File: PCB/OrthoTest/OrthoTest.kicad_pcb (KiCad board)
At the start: 2 copper layers, 233.7 x 127.2 mm, 249 parts, among them SW1 SW_Push, SW10 SW_Push, SW11 SW_Push, SW12 SW_Push, SW13 SW_Push, SW14 SW_Push, SW15 SW_Push, SW16 SW_Push, SW17 SW_Push, SW18 SW_Push, SW19 SW_Push, SW2 SW_Push, SW20 SW_Push, SW21 SW_Push, SW22 SW_Push, SW23 SW_Push, SW24 SW_Push, SW25 SW_Push, SW26 SW_Push, SW27 SW_Push, SW28 SW_Push, SW29 SW_Push, SW3 SW_Push, SW30 SW_Push, SW31 SW_Push, SW32 SW_Push, SW33 SW_Push, SW34 SW_Push, SW35 SW_Push, SW36 SW_Push, SW37 SW_Push, SW38 SW_Push, SW39 SW_Push, SW4 SW_Push, SW40 SW_Push, SW41 SW_Push, SW42 SW_Push, SW43 SW_Push, SW44 SW_Push, SW45 SW_Push, SW46 SW_Push, SW47 SW_Push, SW48 SW_Push, SW49 SW_Push, SW5 SW_Push, SW50 SW_Push, SW51 SW_Push, SW52 SW_Push, SW53 SW_Push, SW54 SW_Push, SW55 SW_Push, SW56 SW_Push, SW57 SW_Push, SW58 SW_Push, SW59 SW_Push, SW6 SW_Push, SW60 RotaryEncoder_Switch_MP, SW61 RotaryEncoder_Switch_MP, SW7 SW_Push, SW8 SW_Push, SW9 SW_Push

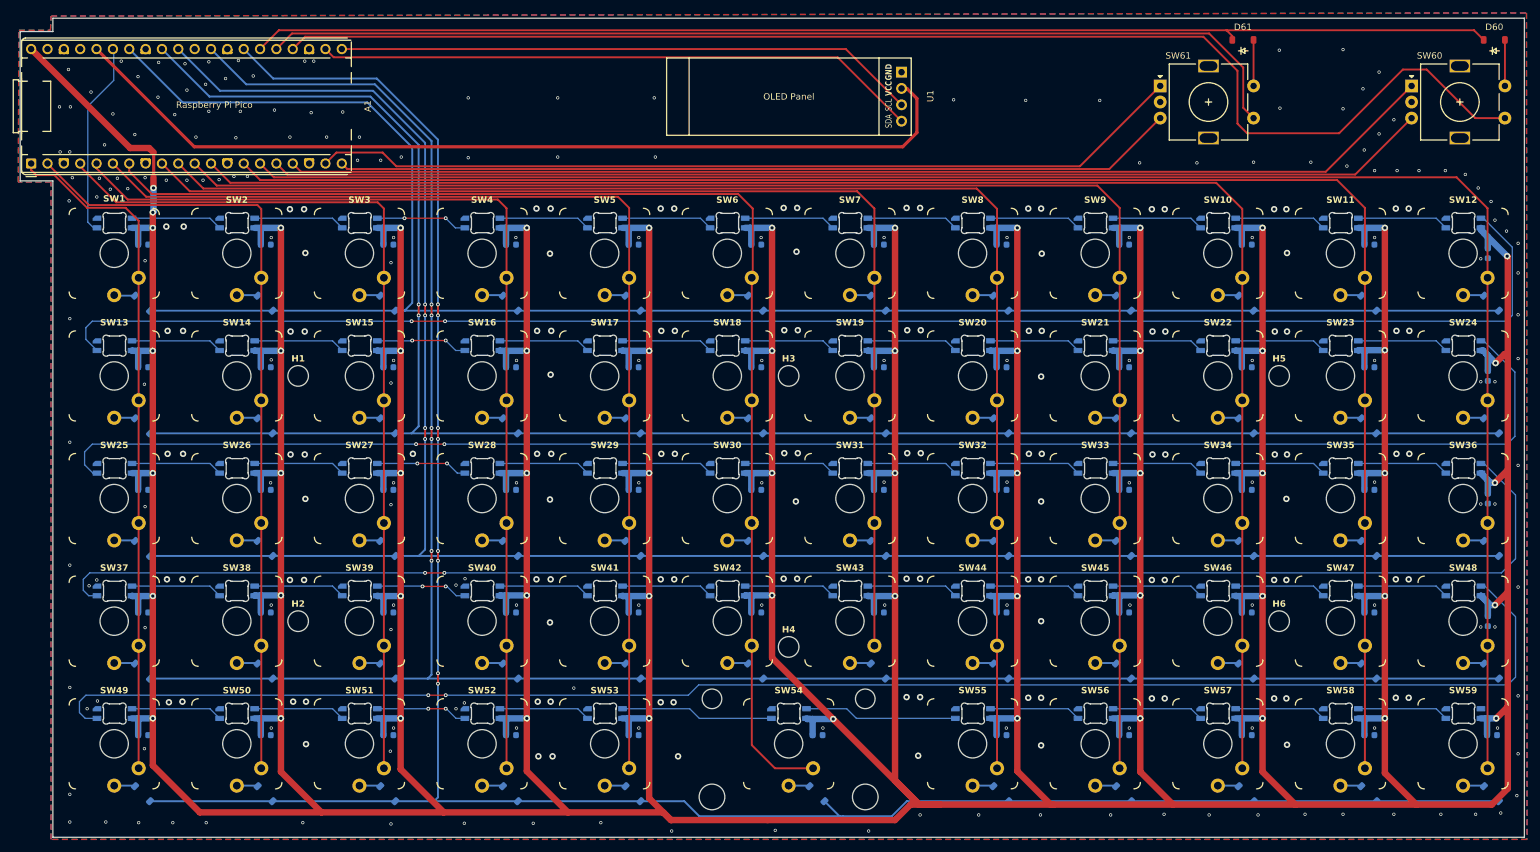
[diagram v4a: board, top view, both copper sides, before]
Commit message: rerouting ucontroller
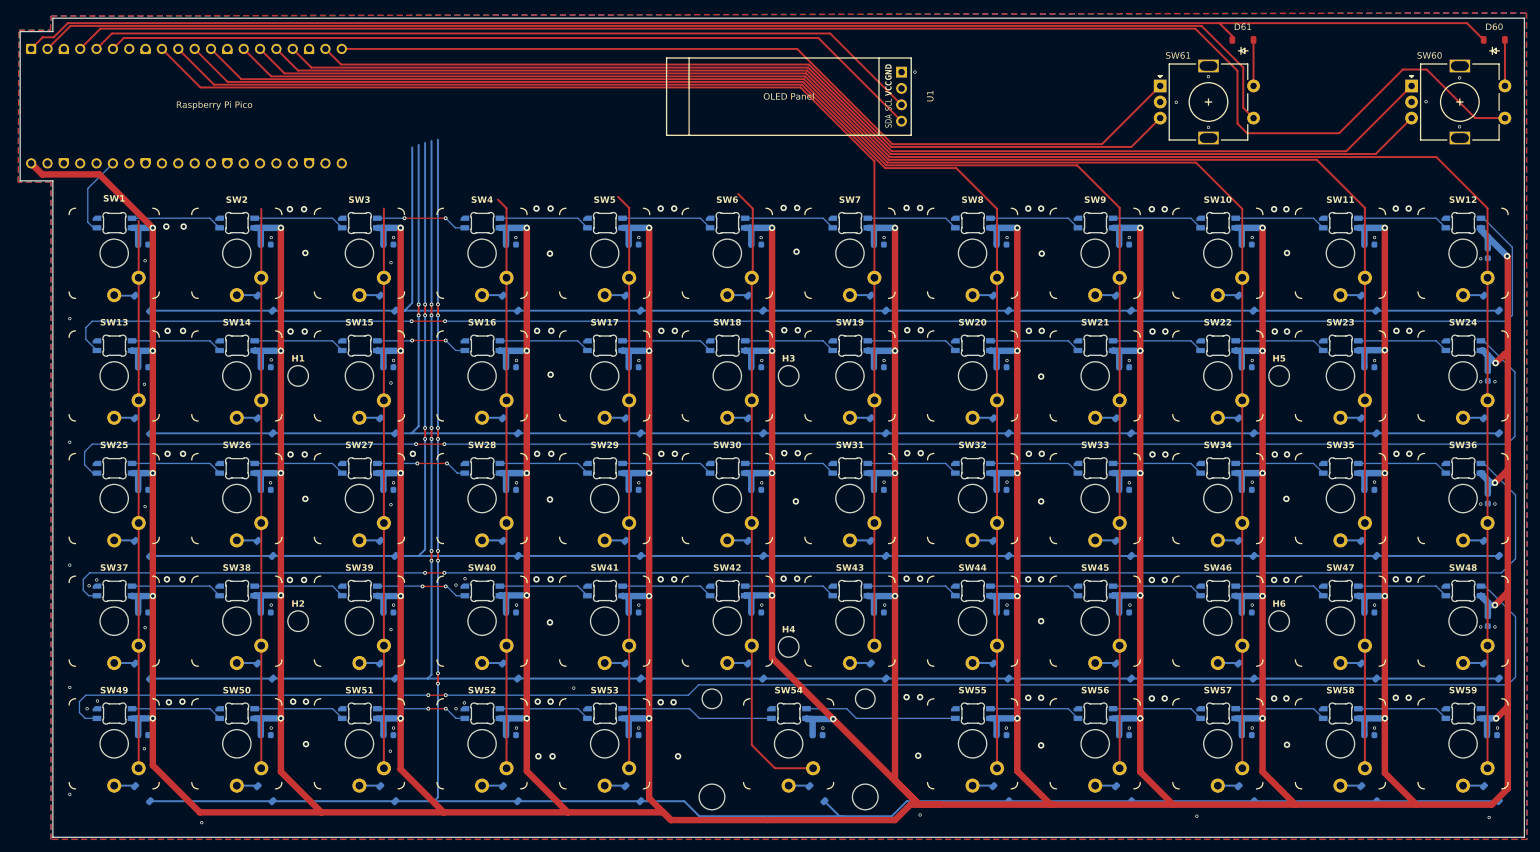
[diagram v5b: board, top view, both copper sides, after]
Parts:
- A1: moved to B.Cu
- moved A1 17.8 mm to (38.7, 35.5), turned to -90 degrees
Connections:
- A1 pad 1: col0 -> ec_row0
- A1 pad 19: ec2_a -> ec2_b
- A1 pad 2: col1 -> ec_col1
- A1 pad 20: ec2_b -> ec2_a
- A1 pad 21: oled_cl -> unconnected-(A1-GPIO16-Pad21)
- A1 pad 22: oled_data -> unconnected-(A1-GPIO17-Pad22)
- A1 pad 24: ec_col0 -> unconnected-(A1-GPIO18-Pad24)
- A1 pad 25: ec_col1 -> unconnected-(A1-GPIO19-Pad25)
- A1 pad 26: ec_row0 -> unconnected-(A1-GPIO20-Pad26)
- A1 pad 4: col2 -> ec_col0
- A1 pad 5: col3 -> oled_cl
- A1 pad 6: col4 -> oled_data
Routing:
- net +3V3: track 143.0 -> 0.00 mm
- net col5: track 194.9 -> 97.6 mm
- net col4: track 170.1 -> 89.5 mm
- net col3: track 154.0 -> 88.9 mm
- net col2: track 137.3 -> 87.0 mm
- net row0: track 285.7 -> 235.4 mm
- net row1: track 300.9 -> 254.8 mm
- net row2: track 318.5 -> 274.1 mm
- net row3: track 333.5 -> 293.3 mm
- net oled_cl: track 90.5 -> 130.6 mm
- net ec_row0: track 193.8 -> 231.8 mm
- net ec_col1: track 161.9 -> 198.4 mm
- net col1: track 123.1 -> 86.9 mm
- net row4: track 353.9 -> 317.9 mm
- net oled_data: track 94.1 -> 128.8 mm
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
